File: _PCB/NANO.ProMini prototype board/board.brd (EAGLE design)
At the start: 85.7 x 100.1 mm, 35 parts, among them T1_5MM 5mm, T2_5MM 5mm, T3_5MM 5mm

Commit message: update
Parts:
- removed 5PIN1, 5PIN2: (no value), SparkFun-Connectors:USB-B-MICRO-SMD
- removed D_5PIN, D_B, J2: (no value), SparkFun-Connectors:1X02_LOCK
- removed VCC: (no value), SparkFun-Connectors:1X04_LOCK_LONGPADS
- added BOARD_POWER: (no value), SparkFun-Connectors:1X04_LOCK_LONGPADS
- added H2, H3: MOUNT-HOLE3.0, holes:3,0
- added J4: (no value), SparkFun-Connectors:1X04_LOCK
- added MICRO_1, MICRO_2: (no value), SparkFun-Connectors:USB-MICROB
- added MINI_1: USB_MINI-B_SMT, SparkFun-Connectors:USB-MINIB
- added PIEZO_: (no value), buzzer:F/CM12P
- added SW1: (no value), special:EDG-04
- added U$1: USB-SERIAL-CP2102, diy-modules:USB-SERIAL-CP2102
- added USB_DATA: (no value), SparkFun-Connectors:1X02_LOCK
- 3.3V, 5V, GND: device pinhead:1X04 -> SparkFun-Connectors:1X05_LOCK_LONGPADS
- PIEZO: device buzzer:F/CM12P -> SparkFun-Connectors:1X02_LOCK
- VIN: device pinhead:1X04 -> SparkFun-Connectors:1X04_LOCK_LONGPADS
- moved RA-02 87.1 mm to (13.7, 12.1)
- moved PIEZO 54.6 mm to (19.6, 46.6)
- moved VIN 24.7 mm to (90.3, 4.06), turned to 0 degrees
- moved T1_5MM 22.1 mm to (80.8, 48.6), turned to 0 degrees
- moved ES32-433T20D 21.5 mm to (16.3, 23.1)
- moved 3.3/5 21.4 mm to (19.4, 42.2)
- moved J1 21.4 mm to (19.4, 23.1)
- moved GND 21.1 mm to (90.4, 8.64), turned to 0 degrees
- moved 5V 21.0 mm to (90.4, 13.3), turned to 0 degrees
- moved 3.3V 21.0 mm to (90.4, 18.0), turned to 0 degrees
- moved PIN1 11.8 mm to (73.2, 47.4), turned to 90 degrees
- moved PH2 10.3 mm to (35.8, 21.1)
- moved PIN2 8.89 mm to (73.2, 36.6)
- moved PIN3 8.89 mm to (73.2, 25.8)
- moved T2_5MM 8.89 mm to (80.8, 37.8)
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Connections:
- removed net GND.3: RA-02.9
- removed net GND.4: RA-02.16
- removed net N$36: D_B.2, USB_B.D+
- removed net N$37: NANO.5V, PH1.23, PH1.24, VCC.3
- new net +5V: U$1.6
- new net 3V3: U$1.1
- new net N$38: BOARD_POWER.3, NANO.5V, PH1.23, PH1.24, SW1.5, SW1.6, SW1.7, SW1.8
- new net N$39: J4.1, SW1.4
- new net N$40: J4.2, SW1.3
- new net N$41: J4.3, SW1.2
- new net N$42: J4.4, SW1.1
- net 3.3V: now also 3.3V.5, BOARD_POWER.2; no longer 3.3V.1, VCC.2
- net 5V: now also 5V.5, BOARD_POWER.4, MICRO_1.VBUS, MICRO_2.VBUS, MINI_1.VBUS; no longer 5PIN1.VBUS, 5PIN2.VBUS, VCC.4
- net D+_5PIN: now also MICRO_1.D+, MICRO_2.D+, MINI_1.D+, USB_B.D+, USB_DATA.2; no longer 5PIN1.D+, 5PIN2.D+, D_5PIN.2
- net D-_5PIN: now also MICRO_1.D-, MICRO_2.D-, MINI_1.D-, USB_B.D-, USB_DATA.1; no longer 5PIN1.D-, 5PIN2.D-, D_5PIN.1
- net GND: now also MICRO_1.GND, MICRO_2.GND, MINI_1.GND, PIEZO_.-, U$1.5; no longer 5PIN1.GND, 5PIN2.GND, GND.1, GND.2, GND.3, GND.4, PIEZO.-
- net N$1: now also RA-02.16, RA-02.9
- net N$34: now also PIEZO.1, PIEZO.2, PIEZO_.+; no longer J2.1, J2.2, PIEZO.+
- net N$35: now also GND.1, GND.2, GND.3, GND.4, GND.5; no longer D_B.1, USB_B.D-
- net SHIELD_IN: now also MICRO_1.MT1, MICRO_1.MT2, MICRO_1.P$1, MICRO_1.P$2, MICRO_2.MT1, MICRO_2.MT2, MICRO_2.P$1, MICRO_2.P$2, MINI_1.S1, MINI_1.S2, MINI_1.S3, MINI_1.S4; no longer 5PIN1.SHIELD1, 5PIN1.SHIELD2, 5PIN1.SHIELD3, 5PIN2.SHIELD1, 5PIN2.SHIELD2, 5PIN2.SHIELD3
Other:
- board text added: "2"
- board text added: "4"
- board text added: "6"
- board text removed: "ICSP2"
- board text removed: "ICSP4"
- board text removed: "ICSP6"
- board text removed: "M3_3MM"

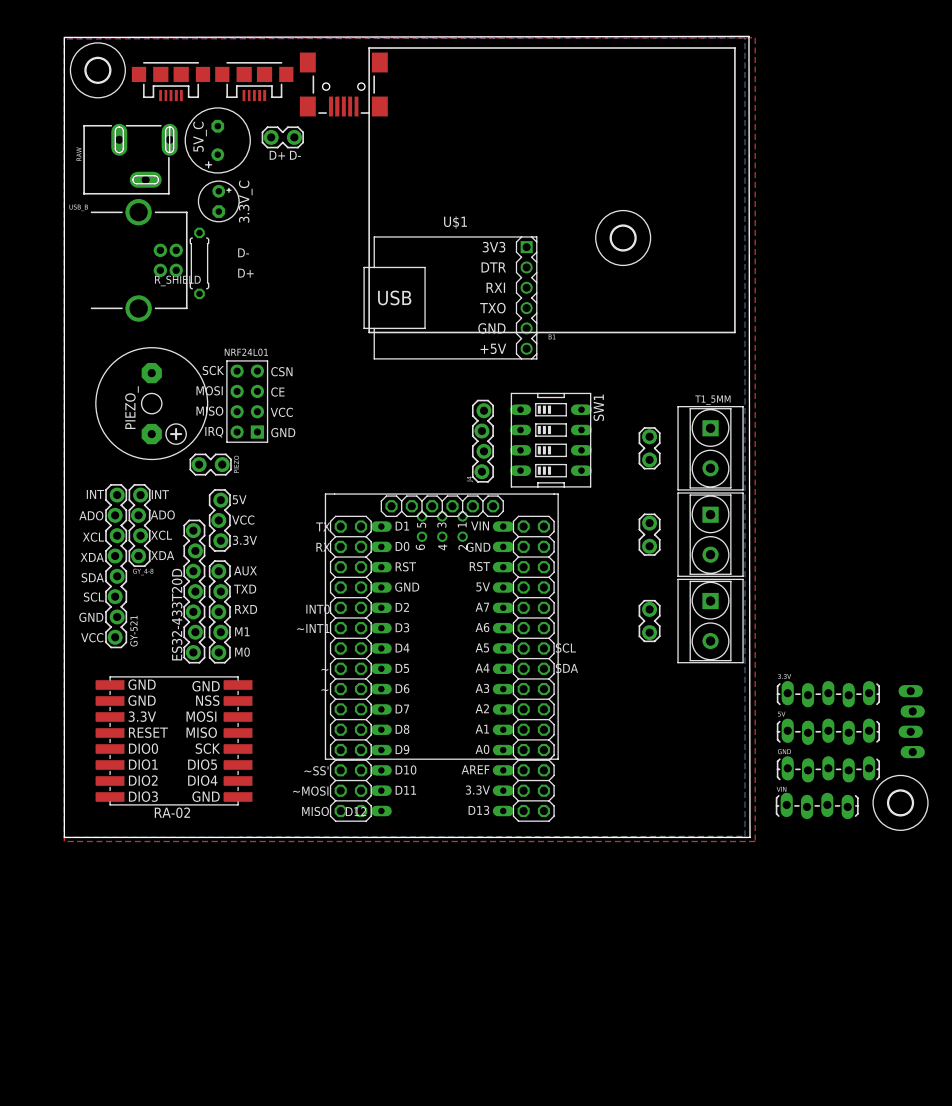
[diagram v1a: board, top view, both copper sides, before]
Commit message: board updates, LoRa
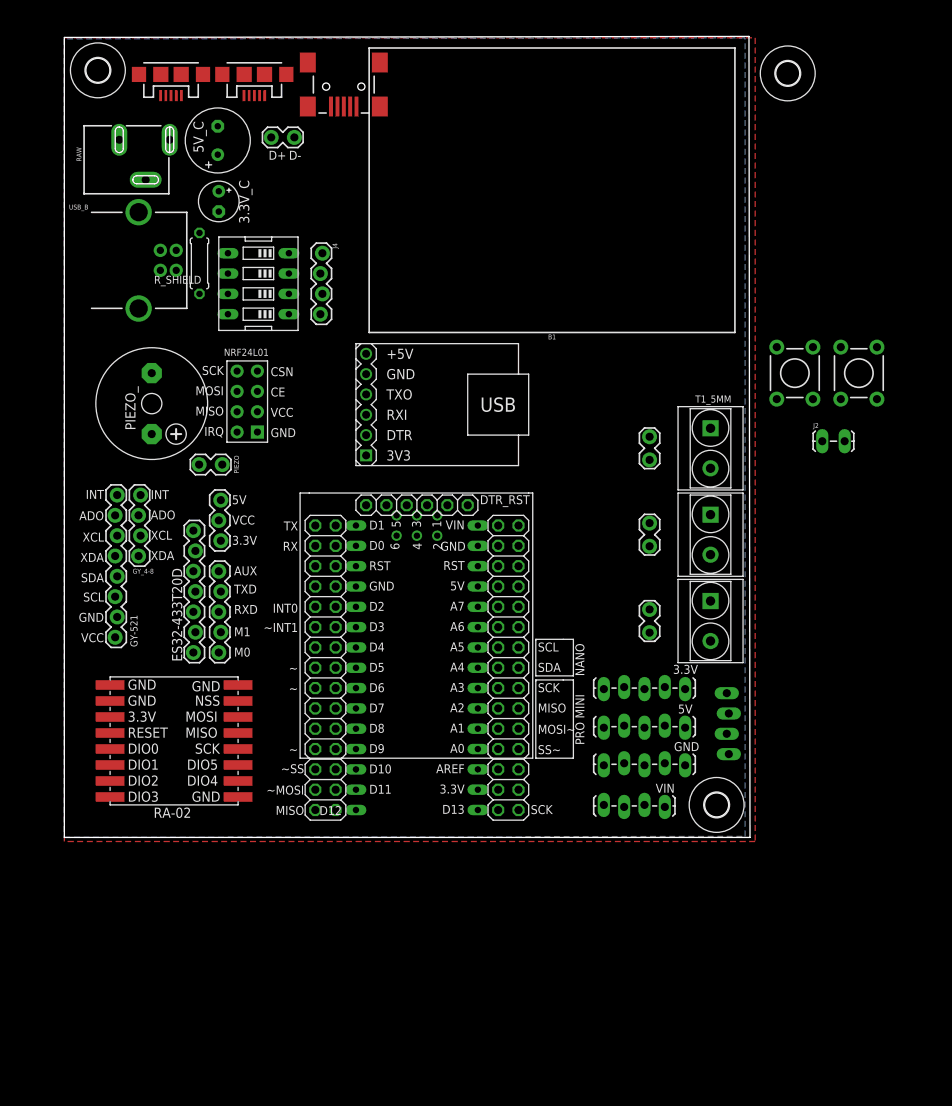
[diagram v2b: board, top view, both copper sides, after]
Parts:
- added J2: (no value), SparkFun-Connectors:1X02_LOCK_LONGPADS
- added S1, S2: MOMENTARY-SWITCH-SPST-PTH-6.0MM, SparkFun-Switches:TACTILE_SWITCH_PTH_6.0MM
- moved SW1 41.5 mm to (24.3, 69.2), turned to 90 degrees
- moved J4 34.0 mm to (32.1, 73.0), turned to 270 degrees
- moved H2 29.1 mm to (90.4, 95.5)
- moved BOARD_POWER 23.0 mm to (82.8, 18.0)
- moved H3 23.0 mm to (81.5, 4.06)
- moved VIN 22.9 mm to (67.4, 4.06)
- moved U$1 13.5 mm to (46.6, 54.1), turned to 180 degrees
- moved 3.3V 12.8 mm to (77.6, 18.5), turned to 180 degrees
- moved 5V 12.8 mm to (77.6, 13.7), turned to 180 degrees
- moved GND 12.8 mm to (77.6, 9.02), turned to 180 degrees
- moved NANO 3.18 mm to (41.5, 30.1)
- moved PH1 3.18 mm to (55.5, 21.2)
- moved PH2 3.18 mm to (32.6, 21.2)
- moved PROMINI_HEADER 3.18 mm to (44.1, 41.5)
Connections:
- removed net N$38: BOARD_POWER.3, NANO.5V, PH1.23, PH1.24, SW1.5, SW1.6, SW1.7, SW1.8
- new net N$36: BOARD_POWER.3, NANO.5V, PH1.23, PH1.24, S1.1, S2.1, SW1.5, SW1.6, SW1.7, SW1.8
- new net N$37: J2.1, S1.3
- new net N$43: J2.2, S2.3
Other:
- board text added: "DTR_RST"
- board text added: "MOSI~"
- board text added: "NANO"
- board text added: "PRO MINI"
- board text added: "SS~"
- board text added: "~SS"
- board text removed: "~SS'"

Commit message: prototype PCB, air mouse example code
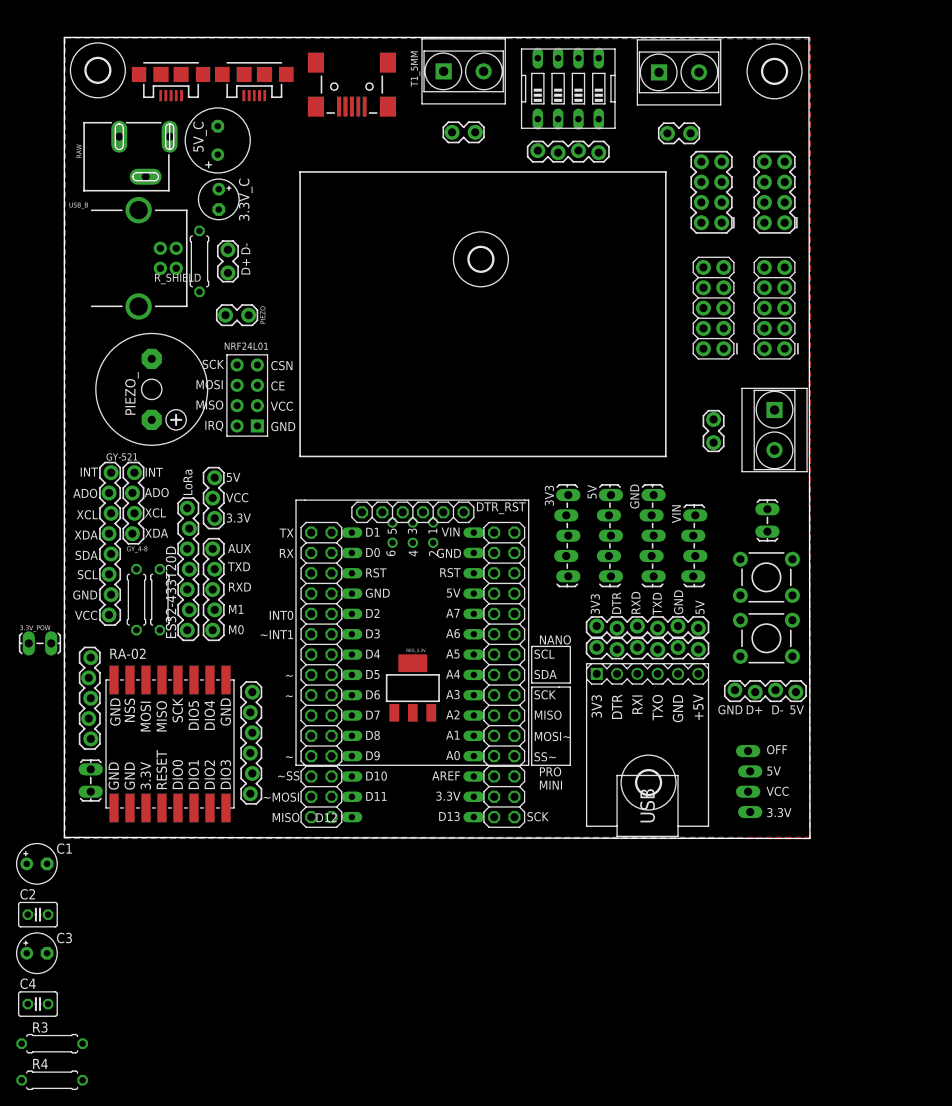
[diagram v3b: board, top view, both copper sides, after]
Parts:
- removed PROMINI_HEADER: (no value), pinhead_v2:1X06/OCT
- removed U$1: USB-SERIAL-CP2102, diy-modules:USB-SERIAL-CP2102
- added 3.3V_POW, J3: (no value), SparkFun-Connectors:1X02_LOCK_LONGPADS
- added C1, C3: (no value), rcl:E2,5-5
- added C2, C4: (no value), rcl:C025-030X050
- added CP2102_USB-SERIAL: (no value), diy-modules:USB-SERIAL-CP2102
- added H4: MOUNT-HOLE3.0, holes:3,0
- added J10, J11: (no value), SparkFun-Connectors:2X4
- added J12, J13: (no value), SparkFun-Connectors:2X5
- added J5, J7, J9: (no value), SparkFun-Connectors:1X06_LOCK
- added J6: (no value), SparkFun-Connectors:1X05_LOCK
- added J8: (no value), SparkFun-Connectors:1X04_LOCK
- added PROMINI_H: (no value), pinhead_v2:1X06/OCT
- added R1: 4.7k, rcl:0207/7
- added R2: 4.7K, rcl:0207/7
- added R3, R4: (no value), rcl:0207/7
- added REG_3.3V: (no value), SparkFun-IC-Power:SOT223
- moved T2_5MM 57.9 mm to (76.8, 95.6), turned to 90 degrees
- moved T1_5MM 56.3 mm to (49.9, 95.8), turned to 90 degrees
- moved PIN2 51.7 mm to (78.1, 88.0), turned to 180 degrees
- moved PIN1 46.3 mm to (51.2, 88.1), turned to 180 degrees
- moved SW1 45.8 mm to (63.0, 93.6), turned to 0 degrees
- moved J4 36.9 mm to (66.8, 85.7), turned to 180 degrees
- moved S2 35.1 mm to (87.8, 24.9), turned to 0 degrees
- moved GND 34.0 mm to (73.7, 42.8), turned to 270 degrees
- moved VIN 30.7 mm to (78.6, 32.6), turned to 90 degrees
- moved 5V 30.5 mm to (68.3, 42.8), turned to 270 degrees
- moved 3.3V 28.3 mm to (63.0, 42.8), turned to 270 degrees
- moved S1 25.8 mm to (87.8, 32.5), turned to 0 degrees
- moved T3_5MM 25.2 mm to (88.8, 50.9)
- moved PIN3 25.1 mm to (81.2, 49.5)
- moved PIEZO 19.0 mm to (22.9, 65.3)
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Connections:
- removed net +5V: U$1.6
- removed net 3V3: U$1.1
- removed net N$1 (its old number): RA-02.1, RA-02.16, RA-02.2, RA-02.9
- new net N$15: ES32-433T20D.4, R1.2
- new net N$38: ES32-433T20D.3, R2.2
- new net N$44: J6.1, RA-02.8
- new net N$45: J6.2, RA-02.7
- new net N$46: J6.3, RA-02.6
- new net N$47: J6.4, RA-02.5
- new net N$48: J6.5, RA-02.4
- new net N$49: J5.1, RA-02.15
- new net N$50: J5.2, RA-02.14
- new net N$51: J5.3, RA-02.13
- new net N$52: J5.4, RA-02.12
- new net N$53: J5.5, RA-02.11
- new net N$54: J5.6, RA-02.10
- new net N$55: J10.1, J11.1
- new net N$56: CP2102_USB-SERIAL.2, J7.2, J9.2, PROMINI_H.6
- new net N$57: CP2102_USB-SERIAL.3, J7.3, J9.3, PROMINI_H.4
- new net N$58: J10.3, J11.3
- new net N$59: J10.5, J11.5
- new net N$60: J10.7, J11.7
- new net N$61: J10.2, J11.2
- new net N$62: CP2102_USB-SERIAL.4, J7.4, J9.4, PROMINI_H.5
- new net N$63: J10.4, J11.4
- new net N$64: J10.6, J11.6
- new net N$65: J10.8, J11.8
- new net N$66: J12.1, J13.1
- new net N$67: J12.3, J13.3
- new net N$68: J12.5, J13.5
- new net N$69: J12.9, J13.9
- new net N$70: J12.7, J13.7
- new net N$71: J12.2, J13.2
- new net N$72: J12.4, J13.4
- new net N$73: J12.6, J13.6
- new net N$74: J12.10, J13.10
- new net N$75: J12.8, J13.8
- new net N$76: J3.2, RA-02.3
- new net N$77: 3.3V_POW.2, C1.+, C2.1, REG_3.3V.3
- new net N$79: R3.1, R4.2, REG_3.3V.1
- net 3.3V: now also BOARD_POWER.4, C3.+, C4.1, CP2102_USB-SERIAL.1, J3.1, J7.1, J9.1, R3.2, REG_3.3V.2, REG_3.3V.4; no longer BOARD_POWER.2, RA-02.3
- net 5V: now also 3.3V_POW.1, BOARD_POWER.2, CP2102_USB-SERIAL.6, J7.6, J8.1, J9.6; no longer BOARD_POWER.4
- net D+_5PIN: now also J8.3
- net D-_5PIN: now also J8.2
- net GND: now also C1.-, C2.2, C3.-, C4.2, CP2102_USB-SERIAL.5, J7.5, J8.4, J9.5, PROMINI_H.1, R4.1, RA-02.1, RA-02.16, RA-02.2, RA-02.9; no longer U$1.5
- net N$13: now also R1.1; no longer ES32-433T20D.4
- net N$14: now also R2.1; no longer ES32-433T20D.3
- net N$36: now also PROMINI_H.3
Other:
- board size 85.7 x 100.1 mm -> 93.2 x 100.1 mm
- board text added: "3V3"
- board text added: "DTR"
- board text added: "LoRa"
- board text added: "OFF"

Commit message: ESP8266 support
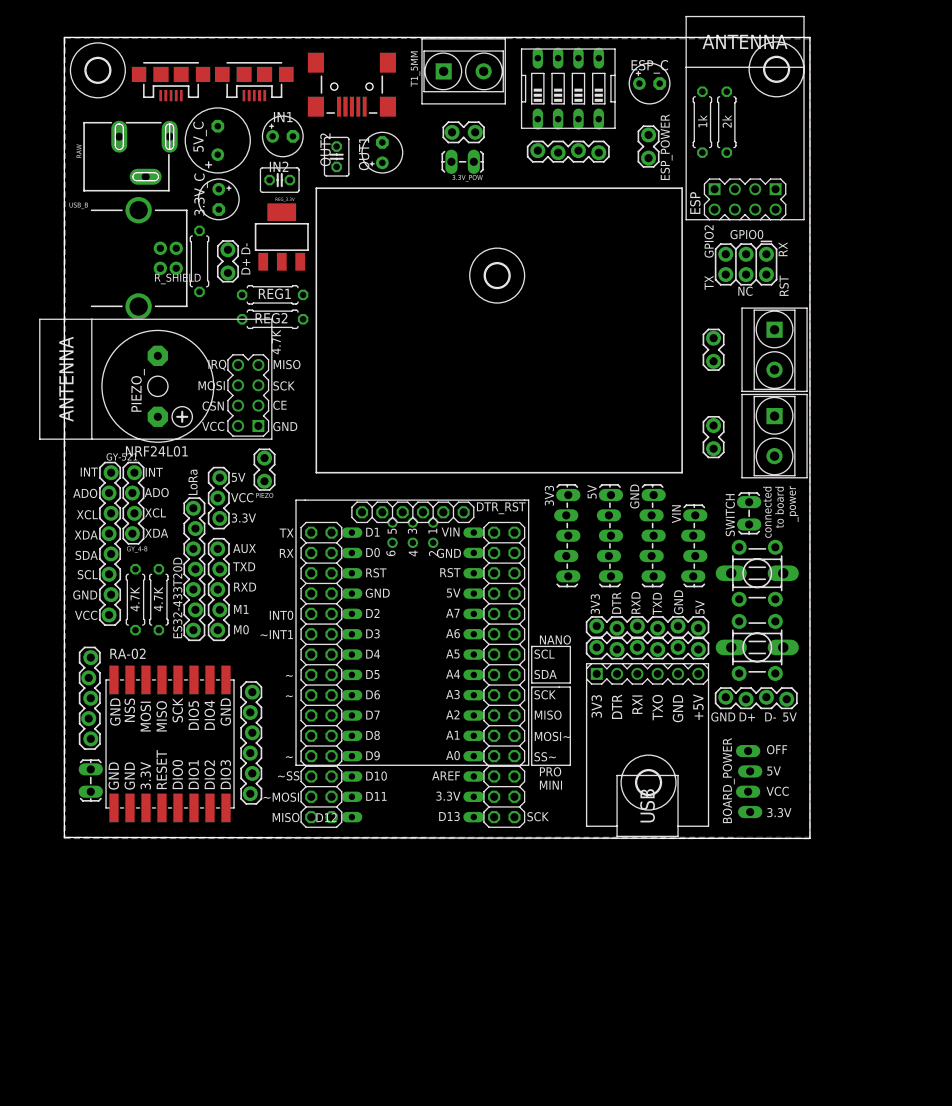
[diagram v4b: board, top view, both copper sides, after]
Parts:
- removed C1, C3: (no value), rcl:E2,5-5
- removed C2, C4: (no value), rcl:C025-030X050
- removed J10, J11: (no value), SparkFun-Connectors:2X4
- removed J12, J13: (no value), SparkFun-Connectors:2X5
- removed R3, R4: (no value), rcl:0207/7
- added ESP: (no value), diy-modules:WIRELESS-WIFI-ESP-01
- added ESP1: 1k, rcl:0207/7
- added ESP2: 2k, rcl:0207/7
- added ESP_C, IN1, OUT1: (no value), rcl:E2,5-5
- added ESP_H: (no value), SparkFun-Connectors:2X3
- added ESP_POW: (no value), SparkFun-Connectors:1X02_LOCK
- added IN2, OUT2: (no value), rcl:C025-030X050
- added REG1, REG2: (no value), rcl:0207/7
- added S3, S4: DTS-3, switch-tact:DTS-3
- NRF24L01: device Seeed-Connector:H2X4-2.54 -> diy-modules:WIRELESS-NRF24L01
- moved 3.3V_POW 81.8 mm to (51.1, 84.5), turned to 180 degrees
- moved REG_3.3V 58.7 mm to (27.2, 75.1)
- moved T2_5MM 36.7 mm to (88.8, 61.0), turned to 0 degrees
- moved PIN2 28.5 mm to (81.2, 59.7), turned to 90 degrees
- moved PIEZO 20.7 mm to (25.0, 44.7), turned to 90 degrees
- moved NRF24L01 11.6 mm to (11.6, 57.8)
- moved B1 2.87 mm to (54.4, 63.4)
- moved H4 2.87 mm to (54.1, 70.2)
- moved J2 2.45 mm to (85.6, 41.8)
- moved S2 1.62 mm to (86.6, 23.7), turned to 270 degrees
- moved J8 1.45 mm to (90.3, 17.4)
- moved S1 1.25 mm to (86.6, 33.0), turned to 270 degrees
- moved PIEZO_ 0.85 mm to (11.7, 56.4)
- moved ES32-433T20D 0.76 mm to (16.3, 25.9)
- moved PIN3 0.76 mm to (81.2, 48.8)
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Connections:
- removed net N$65: J10.8, J11.8
- removed net N$66: J12.1, J13.1
- removed net N$67: J12.3, J13.3
- removed net N$68: J12.5, J13.5
- removed net N$69: J12.9, J13.9
- removed net N$70: J12.7, J13.7
- removed net N$71: J12.2, J13.2
- removed net N$72: J12.4, J13.4
- removed net N$73: J12.6, J13.6
- removed net N$74: J12.10, J13.10
- removed net N$75: J12.8, J13.8
- net 3.3V: now also ESP.D2, ESP_C.+, ESP_POW.1, OUT1.+, OUT2.1, REG1.2; no longer C3.+, C4.1, R3.2
- net GND: now also ESP.A1, ESP2.1, ESP_C.-, IN1.-, IN2.2, OUT1.-, OUT2.2, REG2.1; no longer C1.-, C2.2, C3.-, C4.2, R4.1
- net N$36: now also S3.1, S4.2
- net N$37: now also S3.2
- net N$43: now also S4.1
- net N$55: now also ESP.B2, ESP_POW.2; no longer J10.1, J11.1
- net N$58: now also ESP.D1, ESP1.1, ESP2.2; no longer J10.3, J11.3
- net N$59: now also ESP.C2, ESP_H.2; no longer J10.5, J11.5
- net N$60: now also ESP.C1, ESP_H.3; no longer J10.7, J11.7
- net N$61: now also ESP1.2, ESP_H.1; no longer J10.2, J11.2
- net N$63: now also ESP.B1, ESP_H.5; no longer J10.4, J11.4
- net N$64: now also ESP.A2, ESP_H.6; no longer J10.6, J11.6
- net N$77: now also IN1.+, IN2.1; no longer C1.+, C2.1
- net N$79: now also REG1.1, REG2.2; no longer R3.1, R4.2
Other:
- outline, holes or cut-outs redrawn
- board text added: "1k"
- board text added: "2k"
- board text added: "4.7K"
- board text added: "BOARD_POWER"
- board text added: "ESP_POWER"
- board text added: "GPIO0"
- board text added: "GPIO2"
- board text added: "NC"
- board text added: "SWITCH"
- board text added: "connected to board _power"

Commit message: prototype board finished
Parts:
- removed 3.3V_POW: (no value), SparkFun-Connectors:1X02_LOCK_LONGPADS
- removed ESP: (no value), diy-modules:WIRELESS-WIFI-ESP-01
- removed IN1, OUT1: (no value), rcl:E2,5-5
- removed IN2, OUT2: (no value), rcl:C025-030X050
- removed REG1, REG2: (no value), rcl:0207/7
- removed REG_3.3V: (no value), SparkFun-IC-Power:SOT223
- removed R_SHIELD: 10k, rcl:0207/7
- added ESP8266: (no value), diy-modules:WIRELESS-WIFI-ESP-01
- moved R1 34.7 mm to (45.7, 22.2)
- moved R2 34.7 mm to (42.8, 22.2)
- moved H4 12.3 mm to (54.4, 57.9)
- moved ESP1 3.18 mm to (82.8, 88.5), turned to 270 degrees
- moved ESP2 3.18 mm to (79.8, 88.5)
- moved 3.3V_C 2.05 mm to (21.1, 78.7)
- moved 5V_C 2.05 mm to (21.0, 86.1)
- moved PIEZO_ 1.52 mm to (13.2, 56.4)
- moved NRF24L01 1.52 mm to (13.1, 57.8)
- moved CP2102_USB-SERIAL 1.27 mm to (72.9, 10.3)
- moved H3 1.27 mm to (73.0, 5.59)
- moved J7 1.27 mm to (66.5, 22.5)
- moved J9 1.27 mm to (66.5, 25.1)
- moved MICRO_1 0.89 mm to (24.6, 95.4)
- moved ESP_C 0.68 mm to (73.8, 94.0)
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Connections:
- removed net N$77: 3.3V_POW.2, IN1.+, IN2.1, REG_3.3V.3
- removed net N$79: REG1.1, REG2.2, REG_3.3V.1
- removed net SHIELD_IN: MICRO_1.MT1, MICRO_1.MT2, MICRO_1.P$1, MICRO_1.P$2, MICRO_2.MT1, MICRO_2.MT2, MICRO_2.P$1, MICRO_2.P$2, MINI_1.S1, MINI_1.S2, MINI_1.S3, MINI_1.S4, R_SHIELD.1, USB_B.SHLD1, USB_B.SHLD2
- net 3.3V: now also 3.3V.1, ESP8266.D2; no longer ESP.D2, OUT1.+, OUT2.1, REG1.2, REG_3.3V.2, REG_3.3V.4
- net 5V: no longer 3.3V_POW.1
- net GND: now also ESP8266.A1; no longer ESP.A1, IN1.-, IN2.2, OUT1.-, OUT2.2, REG2.1, R_SHIELD.2
- net N$55: now also ESP8266.B2; no longer ESP.B2
- net N$58: now also ESP8266.D1; no longer ESP.D1
- net N$59: now also ESP8266.C2; no longer ESP.C2
- net N$60: now also ESP8266.C1; no longer ESP.C1
- net N$63: now also ESP8266.B1; no longer ESP.B1
- net N$64: now also ESP8266.A2; no longer ESP.A2
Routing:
- net 3.3V: track 0.00 -> 307.6 mm
- net 5V: track 0.00 -> 235.7 mm, vias 0 -> 4
- net N$36: track 0.00 -> 181.7 mm, vias 0 -> 2
- net D+_5PIN: track 0.00 -> 165.9 mm, vias 0 -> 1
- net D-_5PIN: track 0.00 -> 149.1 mm
- net VIN: track 0.00 -> 110.8 mm
- net SCK_NRF: track 0.00 -> 70.0 mm
- net A5: track 0.00 -> 61.6 mm
- net SDA_GY521: track 0.00 -> 59.6 mm
- net CE_NRF: track 0.00 -> 56.5 mm
- net CSN_NRF: track 0.00 -> 51.3 mm
- net N$57: track 0.00 -> 39.9 mm
- net N$62: track 0.00 -> 39.7 mm
- net N$56: track 0.00 -> 38.9 mm
- net MOSI_NRF: track 0.00 -> 37.0 mm
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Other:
- board text added: "0"
- board text added: "NSS"
- board text added: "RA02 POW"
